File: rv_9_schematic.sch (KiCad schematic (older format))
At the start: 0 parts

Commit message: Working on trim system
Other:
- note added: "Trim"
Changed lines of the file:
@@
 LIBS:contrib
 LIBS:valves
+LIBS:AvionicSchematic
+LIBS:rv_9_schematic-cache
 EELAYER 25 0
 EELAYER END
@@
 Title "RV-9A Schematics"
 Date ""
-Rev ""
+Rev "1"
 Comp ""
 Comment1 ""
@@
 F3 "GND" I L 4050 4050 60
 $EndSheet
+Text Notes 4450 4125 0    60   ~ 0
+Trim
 $EndSCHEMATC

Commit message: Many updates
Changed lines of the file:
@@
 EESchema Schematic File Version 2
+LIBS:rv_9_schematic-rescue
 LIBS:power
 LIBS:device
@@
 $Descr USLetter 11000 8500
 encoding utf-8
-Sheet 1 2
+Sheet 1 3
 Title "RV-9A Schematics"
 Date ""
@@
 S 4050 3650 950  850
 U 5B61469B
-F0 "rv_9_schematic_1" 60
+F0 "Trim System" 60
 F1 "rv_9_schematic_1.sch" 60
 F2 "12V" I L 4050 3850 60
@@
 Text Notes 4450 4125 0    60   ~ 0
 Trim
+$Sheet
+S 5400 3650 1000 850
+U 5B685AE0
+F0 "Lighting" 60
+F1 "rv9_schematic_2.sch" 60
+$EndSheet
 $EndSCHEMATC

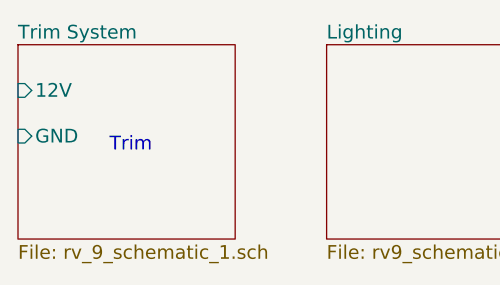
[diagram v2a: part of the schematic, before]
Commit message: Added lighting systems
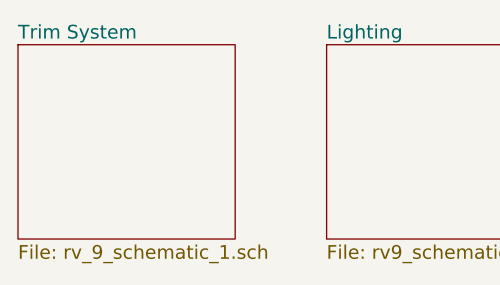
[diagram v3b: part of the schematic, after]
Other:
- note removed: "Trim"
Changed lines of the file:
@@
 EESchema Schematic File Version 2
-LIBS:rv_9_schematic-rescue
 LIBS:power
 LIBS:device
@@
 F0 "Trim System" 60
 F1 "rv_9_schematic_1.sch" 60
-F2 "12V" I L 4050 3850 60
-F3 "GND" I L 4050 4050 60
 $EndSheet
-Text Notes 4450 4125 0    60   ~ 0
-Trim
 $Sheet
 S 5400 3650 1000 850

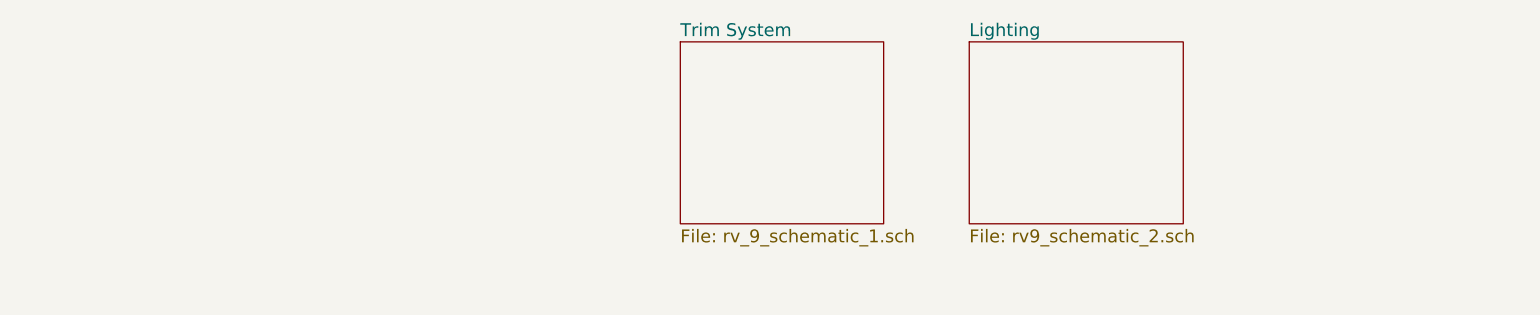
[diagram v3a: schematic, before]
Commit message: Added sheets 3,4,5
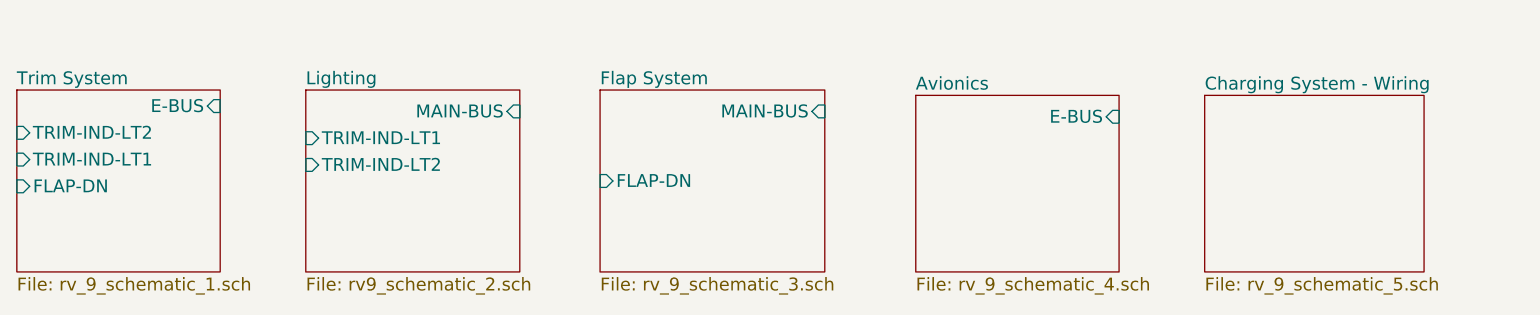
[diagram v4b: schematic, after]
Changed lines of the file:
@@
 $Descr USLetter 11000 8500
 encoding utf-8
-Sheet 1 3
+Sheet 1 6
 Title "RV-9A Schematics"
 Date ""
@@
 $EndDescr
 $Sheet
-S 4050 3650 950  850
+S 950  3875 950  850
 U 5B61469B
 F0 "Trim System" 60
 F1 "rv_9_schematic_1.sch" 60
+F2 "FLAP-DN" I L 950 4325 60
+F3 "TRIM-IND-LT1" I L 950 4200 60
+F4 "TRIM-IND-LT2" I L 950 4075 60
+F5 "E-BUS" I R 1900 3950 60
 $EndSheet
 $Sheet
-S 5400 3650 1000 850
+S 2300 3875 1000 850
 U 5B685AE0
 F0 "Lighting" 60
 F1 "rv9_schematic_2.sch" 60
+F2 "TRIM-IND-LT1" I L 2300 4100 60
+F3 "TRIM-IND-LT2" I L 2300 4225 60
+F4 "MAIN-BUS" I R 3300 3975 60
+$EndSheet
+$Sheet
+S 3675 3875 1050 850
+U 5B79C069
+F0 "Flap System" 60
+F1 "rv_9_schematic_3.sch" 60
+F2 "FLAP-DN" I L 3675 4300 60
+F3 "MAIN-BUS" I R 4725 3975 60
+$EndSheet
+$Sheet
+S 5150 3900 950  825
+U 5B7AF59F
+F0 "Avionics" 60
+F1 "rv_9_schematic_4.sch" 60
+F2 "E-BUS" I R 6100 4000 60
+$EndSheet
+$Sheet
+S 6500 3900 1025 825
+U 5B7B854A
+F0 "Charging System - Wiring" 60
+F1 "rv_9_schematic_5.sch" 60
 $EndSheet
 $EndSCHEMATC
